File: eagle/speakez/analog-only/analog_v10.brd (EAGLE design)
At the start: 100 x 80 mm, 18 parts, among them U1 ADMP621ACEZ-RL7

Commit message: tiny wiring tweak
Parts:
- U1: value ADMP621ACEZ-RL7 -> (none)
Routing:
- net AUDIO: track 6.02 -> 5.39 mm
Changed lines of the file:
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@@
 <element name="R9" library="SparkFun-Resistors" package="0805" value="100k" x="15.24" y="6.35" rot="R90"/>
 <element name="U$1" library="Microchip_By_element14_Batch_1" package="MSOP8" value="MCP6L92" x="22.86" y="11.43"/>
-<element name="U1" library="InvenSense-INMP621ACEZ-R7" package="ADI_ADMP521A" value="ADMP621ACEZ-RL7" x="19.05" y="24.13" rot="R270">
+<element name="U1" library="InvenSense-INMP621ACEZ-R7" package="ADI_ADMP521A" value="" x="19.05" y="24.13" rot="R270">
 <attribute name="MPN" value="ADMP621ACEZ-RL7" x="19.05" y="24.13" size="1.778" layer="27" rot="R270" display="off"/>
 <attribute name="OC_FARNELL" value="2361525 " x="19.05" y="24.13" size="1.778" layer="27" rot="R270" display="off"/>
@@
 <contactref element="C7" pad="1"/>
 <contactref element="R9" pad="1"/>
-<wire x1="19.42" y1="7.62" x2="19.42" y2="5.82" width="0.1524" layer="1"/>
-<wire x1="19.42" y1="5.82" x2="17.78" y2="5.45" width="0.1524" layer="1"/>
 <wire x1="17.78" y1="5.45" x2="15.24" y2="5.45" width="0.1524" layer="1"/>
+<wire x1="17.78" y1="5.45" x2="19.42" y2="7.09" width="0.1524" layer="1"/>
+<wire x1="19.42" y1="7.09" x2="19.42" y2="7.62" width="0.1524" layer="1"/>
 </signal>
 </signals>

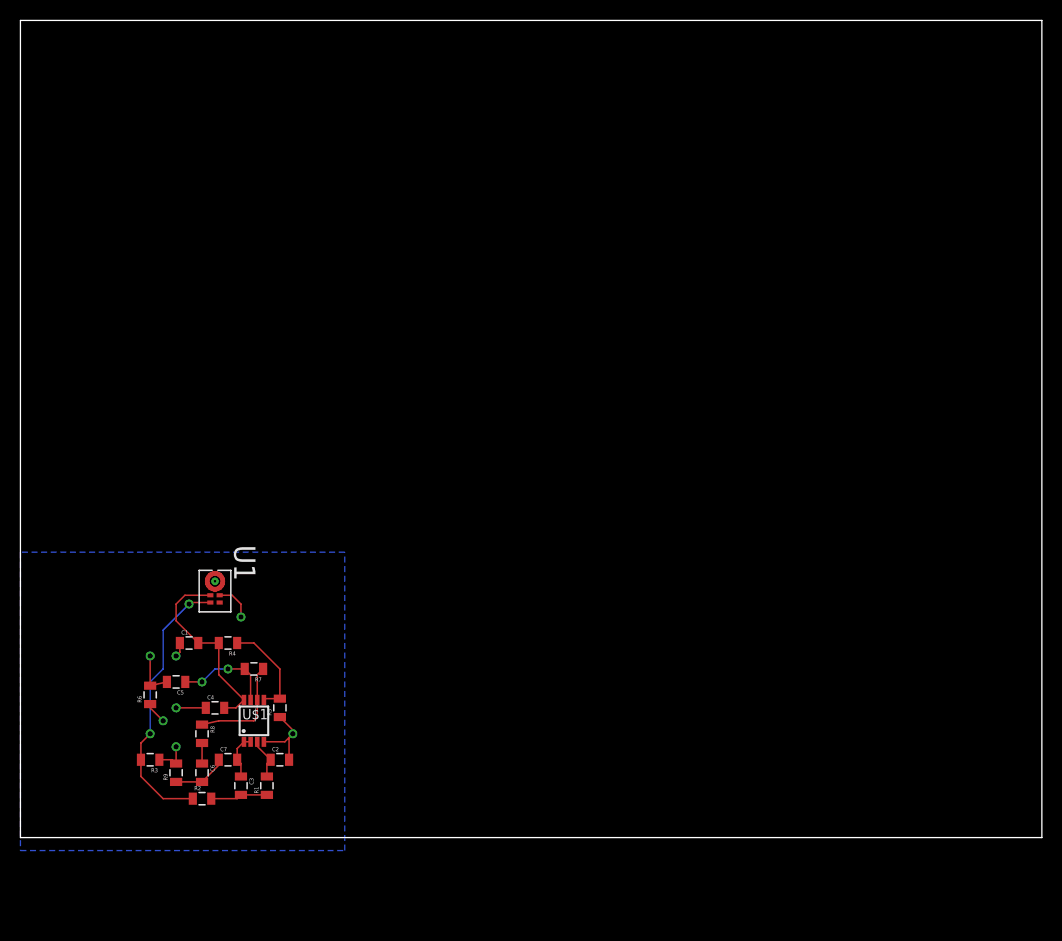
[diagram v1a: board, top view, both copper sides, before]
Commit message: Analog Rev 1
also added a ton of library parts
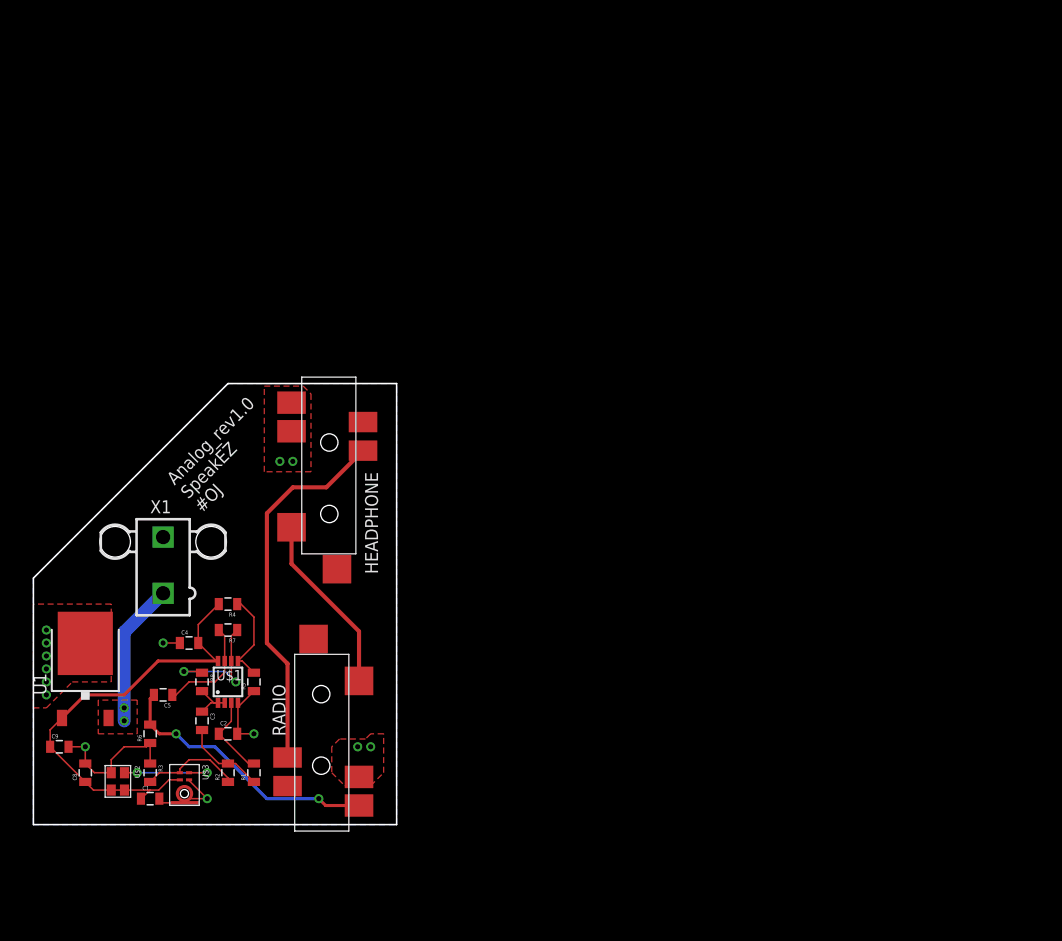
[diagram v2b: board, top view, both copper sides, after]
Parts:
- removed C6, C7: 0.1 uF, SparkFun-Passives:0805
- removed R9: 100k, SparkFun-Resistors:0805
- added C8, C9: 0.1 uF, SparkFun-Passives:0805
- added HEADPHONE, RADIO: SJ-43514-SMT, 35mm_audio:35MM_SMD_4WIRE
- added U$2: SG-210STF, crystal-epson:SG-210STF
- added U$3: INMP621, InvenSense-INMP621ACEZ-R7:CUSTOM_MIC
- added X1: 5566-2, con-molex:5566-2
- C1: value 0.1 uF -> 0.1uF
- U1: value (none) -> +12v; device InvenSense-INMP621ACEZ-R7:ADI_ADMP521A -> LP38691:TO-252
- moved C1 15.7 mm to (12.7, 3.81)
- moved U1 14.8 mm to (6.35, 16.5), turned to 0 degrees
- moved C3 7.41 mm to (17.8, 11.4)
- moved C4 6.84 mm to (16.5, 19.1)
- moved C2 5.68 mm to (20.3, 10.2)
- moved R8 5.08 mm to (17.8, 15.2)
- moved U$1 4.58 mm to (20.3, 15.2)
- moved R7 4.58 mm to (20.3, 20.3)
- moved R6 3.81 mm to (12.7, 10.2)
- moved R4 3.81 mm to (20.3, 22.9)
- moved R5 3.59 mm to (22.9, 15.2)
- moved R2 3.59 mm to (20.3, 6.35), turned to 90 degrees
- moved C5 1.80 mm to (14.0, 14.0)
- moved R1 1.80 mm to (22.9, 6.35)
- moved R3 1.27 mm to (12.7, 6.35), turned to 270 degrees
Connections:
- removed net N$8: C6.1, R8.2
- removed net VOUT_FILTER: C3.1, C7.2, U$1.1, U$1.2
- new net LEFT: HEADPHONE.P$2, RADIO.P$2
- new net RIGHT: HEADPHONE.P$3, RADIO.P$3
- new net VBAT: U1.2, X1.1
- net AUDIO: now also C3.1, R8.2, U$1.1, U$1.2; no longer C6.2, C7.1, R9.1
- net AUDIO_AMPD: now also RADIO.P$1
- net CLK: now also U$2.P$3, U$3.P$1; no longer U1.1
- net GND: now also C1.2, C8.2, C9.2, HEADPHONE.P$1, HEADPHONE.P$4, RADIO.P$4, U$2.P$2, U$3.P$2, U$3.P$3, X1.2; no longer C1.1, R9.2, U1.2, U1.6
- net MIC_PDM: now also U$3.P$5; no longer U1.5
- net VCC: now also C1.1, C8.1, C9.1, U$2.P$1, U$2.P$4, U$3.P$4, U1.1; no longer C1.2, U1.4
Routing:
- net RIGHT: track 0.00 -> 36.7 mm
- net VCC: track 19.3 -> 44.1 mm
- net AUDIO_AMPD: track 4.59 -> 26.8 mm, vias 1 -> 2
- net LEFT: track 0.00 -> 17.8 mm
- net MIC_PDM: track 27.0 -> 9.86 mm, vias 2 -> 0
- net VBAT: track 0.00 -> 14.1 mm, vias 0 -> 2
- net CLK: track 0.00 -> 9.88 mm, vias 0 -> 2
- net GND: track 21.7 -> 30.4 mm, vias 6 -> 14
- net VOUT_FILTER: track 4.48 -> 0.00 mm
- net N$2: track 4.10 -> 8.18 mm
- net N$3: track 5.60 -> 8.14 mm
- net N$7: track 10.6 -> 12.8 mm, vias 0 -> 2
- net N$8: track 2.01 -> 0.00 mm
- net VOUT_AMP: track 9.61 -> 10.4 mm, vias 2 -> 0
- net AUDIO: track 5.39 -> 4.61 mm
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- added copper zone on layer 1, net GND
- added copper zone on layer 1, net VBAT
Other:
- board size 100 x 80 mm -> 35.6 x 43.2 mm
- board text added: "Analog_rev1.0 SpeakEZ #OJ"

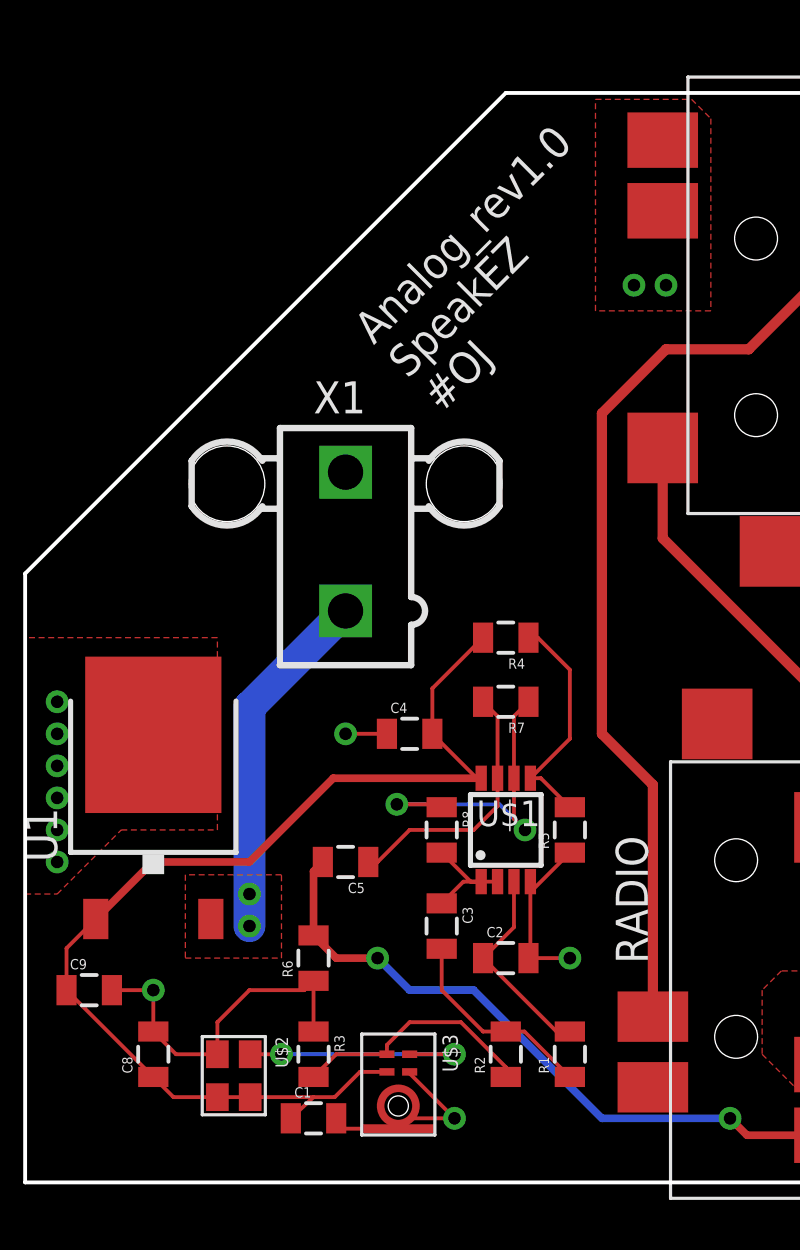
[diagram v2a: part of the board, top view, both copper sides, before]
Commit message: Safety diode
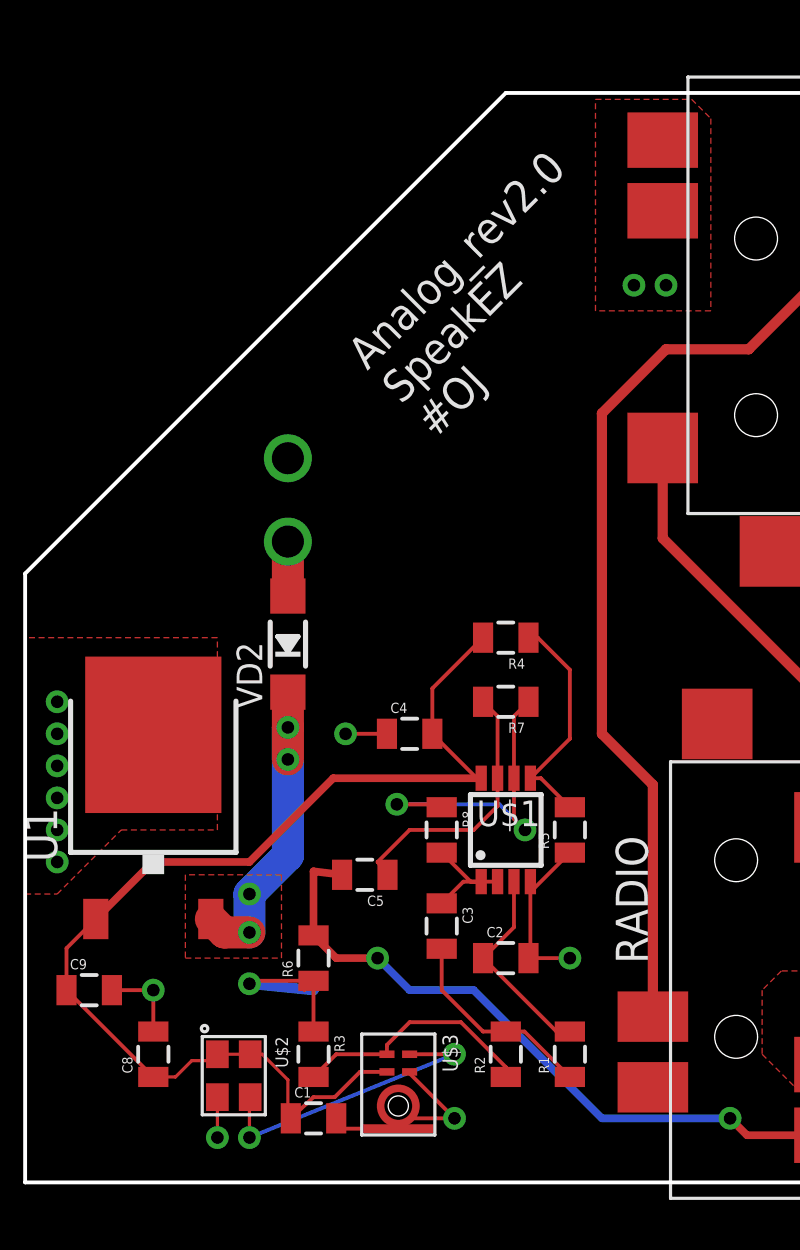
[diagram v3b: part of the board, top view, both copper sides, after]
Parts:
- removed X1: 5566-2, con-molex:5566-2
- added VD2: (no value), diode:SOD123
- moved C5 0.92 mm to (14.7, 13.5)
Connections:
- new net VBATSAFE: U1.2, VD2.C
- net CLK: now also U$2.CLK; no longer U$2.P$3
- net GND: now also U$2.GND; no longer U$2.P$2, X1.2
- net VBAT: now also VD2.A; no longer U1.2, X1.1
- net VCC: now also U$2.ST, U$2.VCC; no longer U$2.P$1, U$2.P$4
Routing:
- net VBATSAFE: track 0.00 -> 13.2 mm, vias 0 -> 4
- net VBAT: track 14.1 -> 2.16 mm, vias 2 -> 1
- net CLK: track 9.88 -> 12.2 mm
- net VCC: track 44.1 -> 45.1 mm
- net GND: track 30.4 -> 29.4 mm, vias 14 -> 17
- net AUDIO_AMPD: track 26.8 -> 27.4 mm
- added copper zone on layer 1, net VBATSAFE
- removed copper zone on layer 1, net VBAT
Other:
- board text added: "Analog_rev2.0 SpeakEZ #OJ"
- board text removed: "Analog_rev1.0 SpeakEZ #OJ"

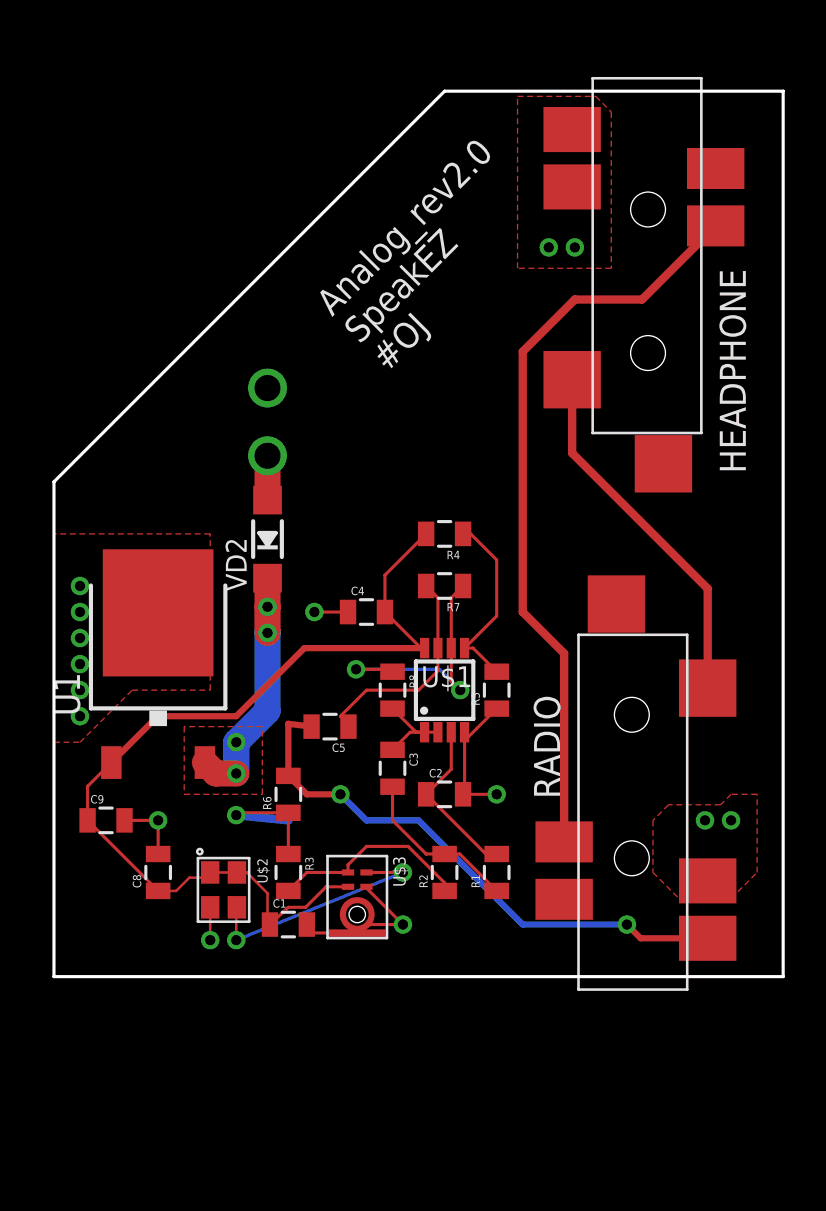
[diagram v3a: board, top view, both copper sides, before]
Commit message: Added headers for mic
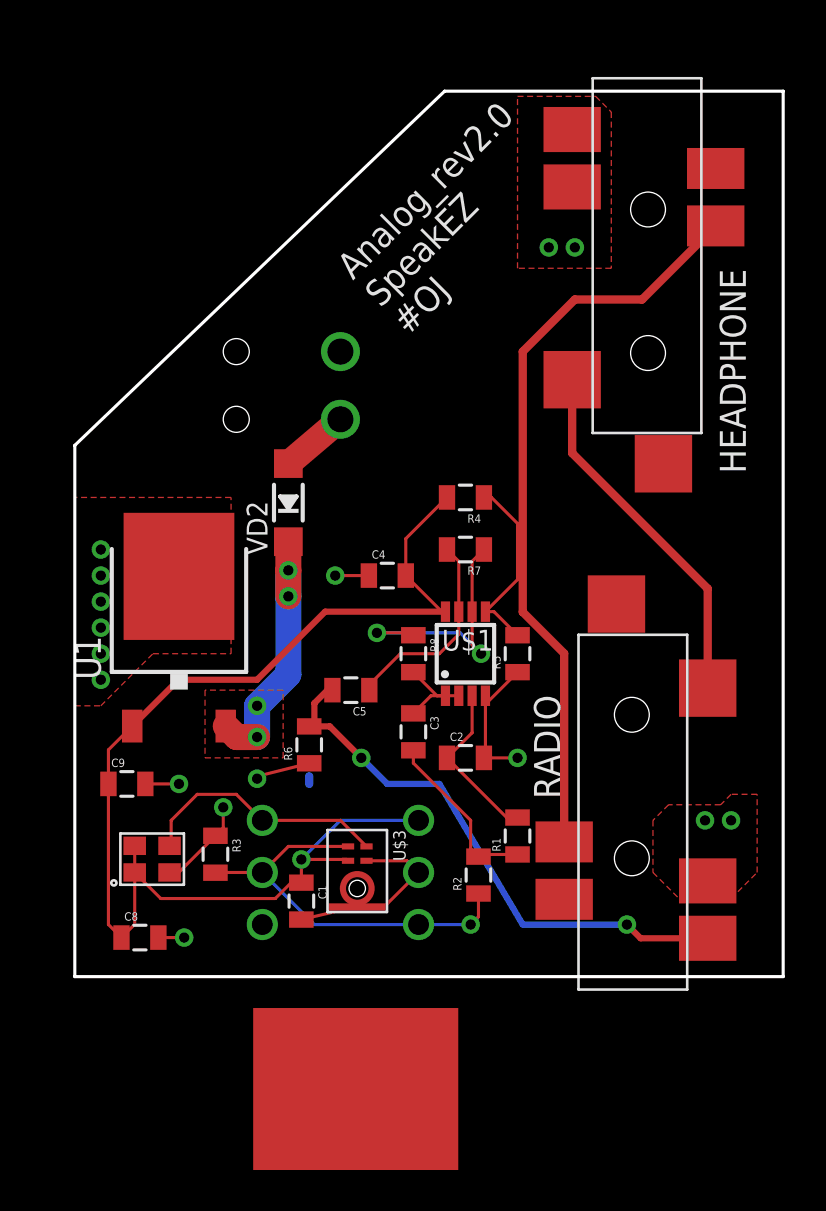
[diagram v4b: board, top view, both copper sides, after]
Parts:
- moved U$2 3.68 mm to (5.21, 6.35), turned to 0 degrees
- moved R3 3.67 mm to (9.14, 7.24)
- moved C8 3.30 mm to (5.46, 3.17), turned to 0 degrees
- moved R6 2.62 mm to (13.7, 12.6)
- moved R1 2.05 mm to (23.9, 8.13)
- moved R4 2.05 mm to (21.3, 24.6)
- moved R5 2.05 mm to (23.9, 17.0)
- moved C5 2.05 mm to (15.7, 15.2)
- moved C2 2.05 mm to (21.3, 11.9)
- moved C3 2.05 mm to (18.8, 13.2)
- moved R8 2.05 mm to (18.8, 17.0)
- moved U$1 2.05 mm to (21.3, 17.0)
- moved U1 2.05 mm to (7.37, 18.3)
- moved VD2 2.05 mm to (12.7, 24.4)
- moved C9 2.05 mm to (4.83, 10.7)
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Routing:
- net VCC: track 45.1 -> 59.4 mm, vias 0 -> 2
- net MIC_PDM: track 9.86 -> 19.9 mm, vias 0 -> 2
- net VBAT: track 2.16 -> 3.33 mm
- net GND: track 29.4 -> 28.3 mm, vias 17 -> 19
- net VOUT_AMP: track 10.7 -> 9.97 mm
- net CLK: track 12.2 -> 12.4 mm, vias 2 -> 1
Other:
- board size 35.6 x 43.2 mm -> 34.5 x 43.2 mm
